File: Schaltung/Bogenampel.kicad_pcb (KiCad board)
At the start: 2 copper layers, 95 x 62 mm, 32 parts, among them J1 Input 1, J10 Display, J2 Input 2, J3 Input 3, J4 Input 4, J5 Input 5, J6 Power Bank, J7 Battery, J8 KY-006, J9 WS2812B Stripe Timer, U1 NRF24L01_Breakout, U2 TXS0108EPW

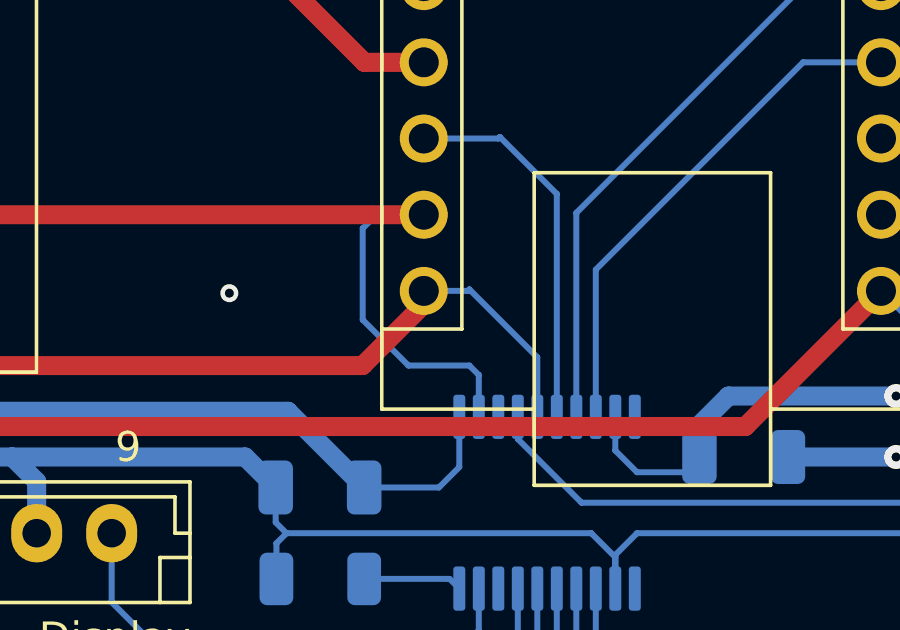
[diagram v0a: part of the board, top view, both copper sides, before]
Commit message: Fix: NRF24L01 Funkverbindung - Konfiguration korrigiert
Mehrere kritische Probleme behoben:

1. Payload-Größe synchronisiert
   - Sender: 4 Bytes → 2 Bytes (passend zu RadioPacket)
   - Empfänger: bereits korrekt 2 Bytes

2. Pin-Initialisierung korrigiert
   - Entfernt manuelle CE/CSN Pin-Init (RF24.begin() macht das)
   - Verhindert Konflikte mit RF24-Bibliothek

3. SPI-Bus-Initialisierung optimiert (Sender)
   - SPI.begin() einmal am Anfang von setup()
   - Radio VOR Display initialisieren (verhindert SPI-Konflikte)
   - Doppelte SPI.begin() Aufrufe entfernt

4. RF24-Enums direkt verwendet
   - Entfernt custom DataRate/PowerLevel Enums
   - Verwendet rf24_datarate_e und rf24_pa_dbm_e direkt
   - Behebt Type-Cast Probleme

5. Namenskonflikte behoben
   - Groups::Type::CD → Groups::Type::GROUP_CD
   - Konflikt mit RF24 Makro #define CD 0x09

6. Debug-Ausgaben erweitert
   - Manuelle Radio-Diagnose hinzugefügt
   - isChipConnected(), getChannel(), etc.

Hardware-Problem identifiziert:
- NRF24L01 benötigt 3.3V (nicht 5V!)
- Kondensator 10-100µF empfohlen
- Evtl. Level-Shifter für 5V↔3.3V Logik nötig

🤖 Generated with [Claude Code](https://claude.com/claude-code)

Co-Authored-By: Claude Sonnet 4.5 <noreply@anthropic.com>
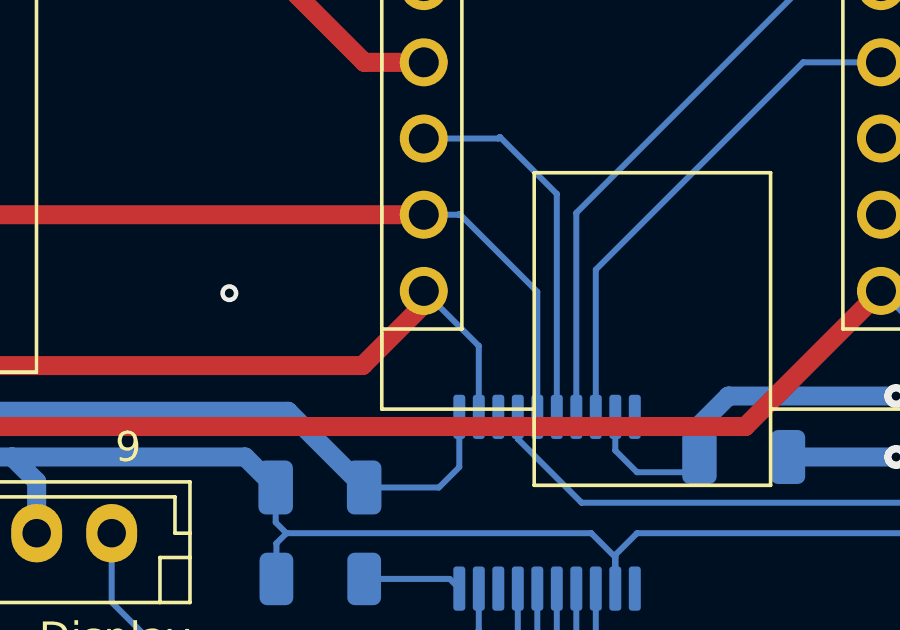
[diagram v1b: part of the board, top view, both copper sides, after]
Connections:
- A2 pad 14: /SPI.MISO -> /SPI.MOSI
- A2 pad 15: /SPI.MOSI -> /SPI.MISO
- U1 pad 6: /SPI.MISO -> /SPI.MOSI
- U1 pad 7: /SPI.MOSI -> /SPI.MISO
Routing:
- net /SPI.MOSI: track 52.9 -> 48.3 mm
- net /SPI.MISO: track 50.6 -> 51.1 mm
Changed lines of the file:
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@@
 			(layers "*.Cu" "*.Mask")
 			(remove_unused_layers no)
-			(net 5 "/SPI.MISO")
+			(net 21 "/SPI.MOSI")
 			(pinfunction "MOSI")
 			(pintype "input")
@@
 			(layers "*.Cu" "*.Mask")
 			(remove_unused_layers no)
-			(net 21 "/SPI.MOSI")
+			(net 5 "/SPI.MISO")
 			(pinfunction "MISO")
 			(pintype "output")
@@
 			(layers "*.Cu" "*.Mask")
 			(remove_unused_layers no)
-			(net 5 "/SPI.MISO")
+			(net 21 "/SPI.MOSI")
 			(pinfunction "D11")
 			(pintype "bidirectional")
@@
 			(layers "*.Cu" "*.Mask")
 			(remove_unused_layers no)
-			(net 21 "/SPI.MOSI")
+			(net 5 "/SPI.MISO")
 			(pinfunction "D12")
 			(pintype "bidirectional")
@@
 	)
 	(segment
-		(start 100.263 86.439)
-		(end 98.6865 86.439)
+		(start 136.656 92)
+		(end 136.656 92.452)
 		(width 0.635)
 		(layer "F.Cu")
@@
 	)
 	(segment
-		(start 103.284 89.46)
-		(end 100.263 86.439)
+		(start 98.152 94.488)
+		(end 96.1465 92.4825)
 		(width 0.635)
 		(layer "F.Cu")
@@
 	)
 	(segment
-		(start 136.656 89.46)
-		(end 103.284 89.46)
+		(start 134.62 94.488)
+		(end 98.152 94.488)
 		(width 0.635)
 		(layer "F.Cu")
@@
 	)
 	(segment
-		(start 135.18 89.46)
-		(end 136.656 89.46)
-		(width 0.2)
-		(layer "B.Cu")
-		(net 5)
-	)
-	(segment
-		(start 138.49 94.802)
-		(end 138.176 94.488)
-		(width 0.2)
-		(layer "B.Cu")
-		(net 5)
-	)
-	(segment
-		(start 134.62 92.964)
-		(end 134.62 89.916)
-		(width 0.2)
-		(layer "B.Cu")
-		(net 5)
-	)
-	(segment
-		(start 134.62 89.916)
-		(end 135.128 89.408)
-		(width 0.2)
-		(layer "B.Cu")
+		(start 136.656 92.452)
+		(end 134.62 94.488)
+		(width 0.635)
+		(layer "F.Cu")
 		(net 5)
 	)
 	(segment
-		(start 135.128 89.408)
-		(end 135.18 89.46)
-		(width 0.2)
-		(layer "B.Cu")
+		(start 96.1465 92.4825)
+		(end 96.1465 88.979)
+		(width 0.635)
+		(layer "F.Cu")
 		(net 5)
 	)
 	(segment
 		(start 138.49 96.1975)
-		(end 138.49 94.802)
-		(width 0.2)
-		(layer "B.Cu")
-		(net 5)
-	)
-	(segment
-		(start 138.176 94.488)
-		(end 136.144 94.488)
+		(end 138.49 93.834)
 		(width 0.2)
 		(layer "B.Cu")
@@
 	)
 	(segment
-		(start 136.144 94.488)
-		(end 134.62 92.964)
+		(start 138.49 93.834)
+		(end 136.656 92)
 		(width 0.2)
 		(layer "B.Cu")
@@
 	)
 	(segment
-		(start 136.656 92)
-		(end 136.656 92.452)
-		(width 0.635)
-		(layer "F.Cu")
-		(net 21)
-	)
-	(segment
-		(start 98.152 94.488)
-		(end 96.1465 92.4825)
-		(width 0.635)
-		(layer "F.Cu")
-		(net 21)
-	)
-	(segment
-		(start 134.62 94.488)
-		(end 98.152 94.488)
+		(start 100.263 86.439)
+		(end 98.6865 86.439)
 		(width 0.635)
 		(layer "F.Cu")
@@
 	)
 	(segment
-		(start 136.656 92.452)
-		(end 134.62 94.488)
+		(start 103.284 89.46)
+		(end 100.263 86.439)
 		(width 0.635)
 		(layer "F.Cu")
@@
 	)
 	(segment
-		(start 96.1465 92.4825)
-		(end 96.1465 88.979)
+		(start 136.656 89.46)
+		(end 103.284 89.46)
 		(width 0.635)
 		(layer "F.Cu")
@@
 	)
 	(segment
-		(start 138.176 91.948)
-		(end 138.124 92)
+		(start 137.8458 89.4334)
+		(end 137.8192 89.46)
 		(width 0.2)
 		(layer "B.Cu")
@@
 	)
 	(segment
-		(start 138.124 92)
-		(end 136.656 92)
+		(start 137.8192 89.46)
+		(end 136.656 89.46)
 		(width 0.2)
 		(layer "B.Cu")
@@
 	)
 	(segment
-		(start 140.44 96.1975)
-		(end 140.44 94.212)
+		(start 140.44 92.0276)
+		(end 137.8458 89.4334)
 		(width 0.2)
 		(layer "B.Cu")
@@
 	)
 	(segment
-		(start 140.44 94.212)
-		(end 138.176 91.948)
+		(start 140.44 96.1975)
+		(end 140.44 92.0276)
 		(width 0.2)
 		(layer "B.Cu")

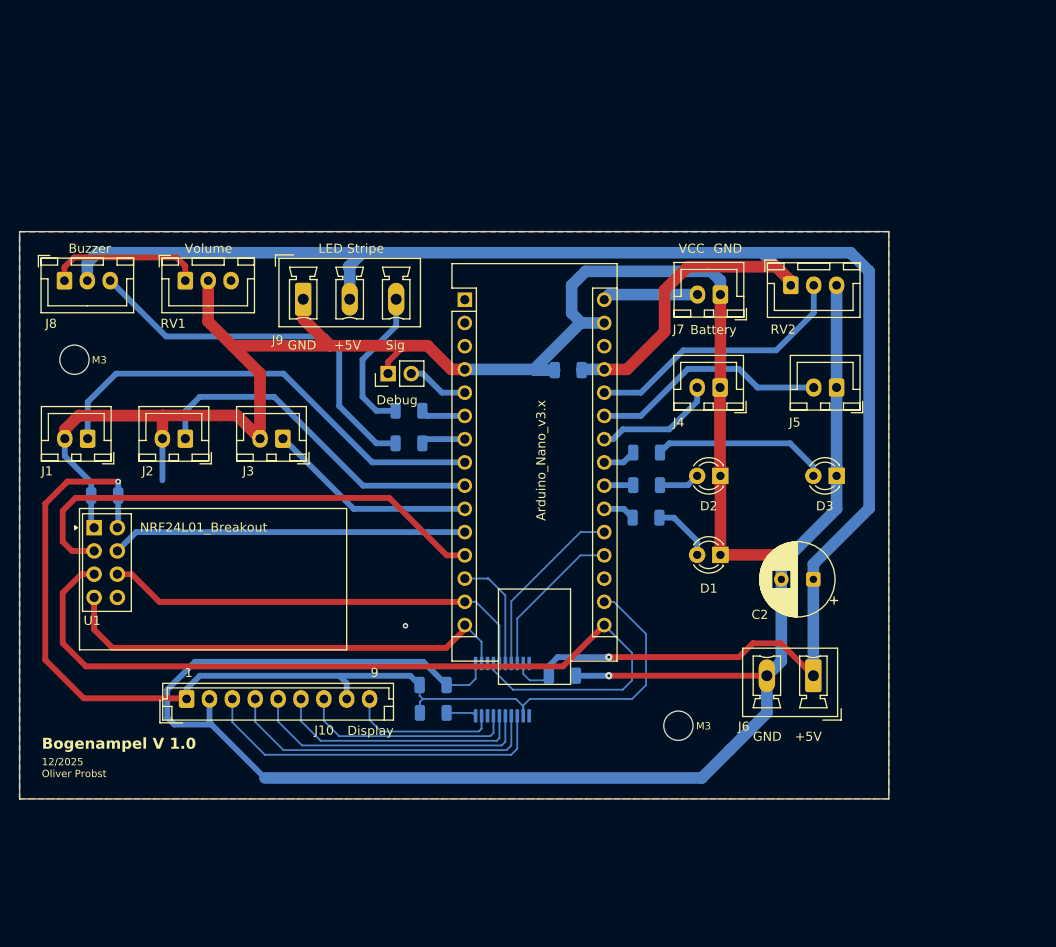
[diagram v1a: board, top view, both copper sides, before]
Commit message: UI-Verbesserungen und Funk-Debugging
Schießbetrieb UI:
- Überschrift in Orange mit Trennlinie
- Timer horizontal zentriert und nur 1x pro Sekunde aktualisiert
- Layout-Abstände optimiert (weniger gestaucht)
- Button "Passe beenden" mit grauem Hintergrund
- Bei 3-4 Schützen: Timer tiefer positioniert

Gruppenanzeige:
- Vereinheitlichtes Format für PfeileHolenMenu und Schießbetrieb
- Statischer String "{A/B -> C/D} {C/D -> A/B}"
- Aktuelle Gruppe gelb hervorgehoben, Rest grau
- "Nächste:" in PfeileHolenMenu, "Aktuell:" in Schießbetrieb

Funk-Debugging:
- Kontinuierliche PING-Tests im Splash Screen (alle 2 Sek)
- Pipe-Adresse wird beim Start ausgegeben
- Versucht printDetails() mit Serial.flush()
- Empfänger auf Pipe 1 umgestellt (statt Pipe 0)

🤖 Generated with [Claude Code](https://claude.com/claude-code)

Co-Authored-By: Claude Sonnet 4.5 <noreply@anthropic.com>
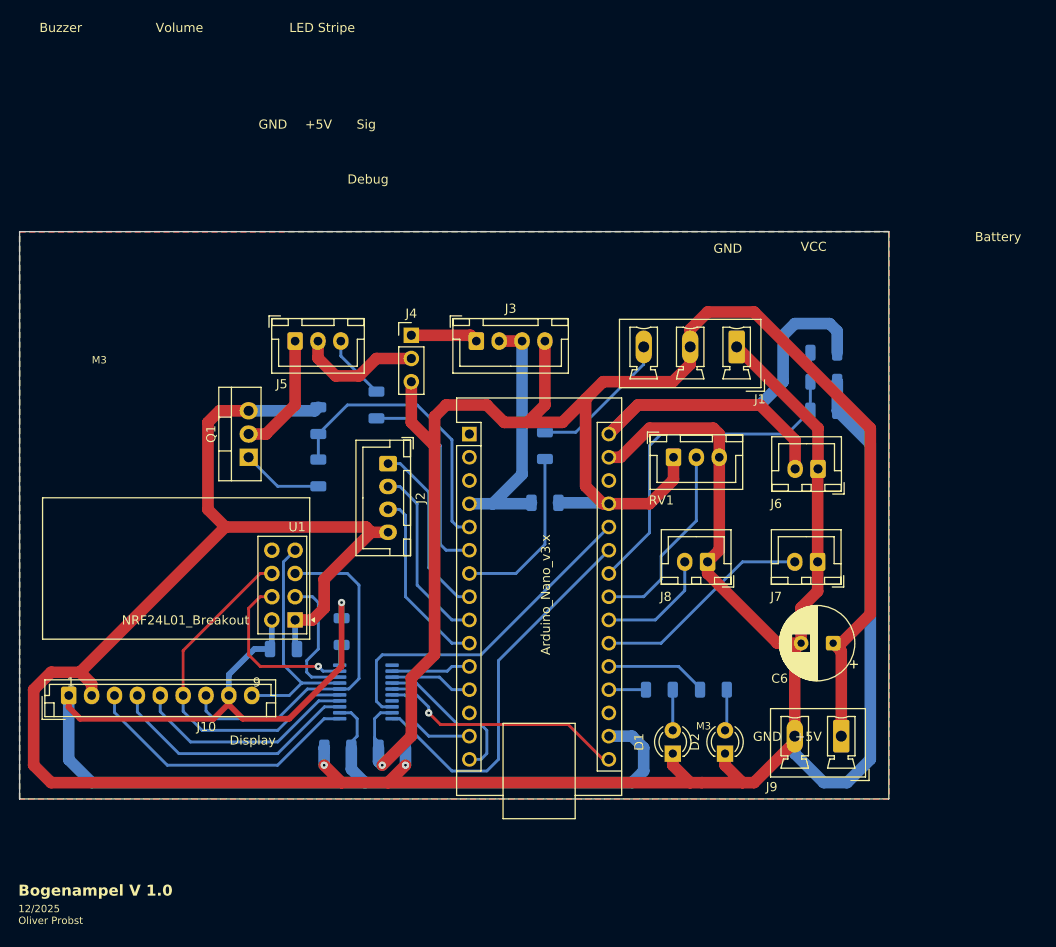
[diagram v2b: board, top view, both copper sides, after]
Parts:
- removed D3: LED, LED_THT:LED_D3.0mm
- removed the J9 at (119.0, 56.4)
- removed JD1: Debug, Connector_PinHeader_2.54mm:PinHeader_1x02_P2.54mm_Vertical
- removed REF** (x2): MountingHole_3.2mm_M3_ISO14580, MountingHole:MountingHole_3.2mm_M3_ISO14580
- removed RV2: Input 6, Connector_JST:JST_XH_B3B-XH-A_1x03_P2.50mm_Vertical
- added C3: 100nF, Capacitor_SMD:C_1206_3216Metric, B.Cu at (175.9, 68.6)
- added J4: Jumper: 5V/Ext Voltage, Connector_PinHeader_2.54mm:PinHeader_1x03_P2.54mm_Vertical, F.Cu at (130.8, 60.3)
- added Q1: IRLZ44N, Package_TO_SOT_THT:TO-220-3_Vertical, F.Cu at (113.0, 73.7)
- added R2: 100Ω, Resistor_SMD:R_1206_3216Metric, B.Cu at (127.0, 67.9)
- added R7: 10kΩ, Resistor_SMD:R_1206_3216Metric, B.Cu at (175.9, 62.2)
- added R8: 10kΩ, Resistor_SMD:R_1206_3216Metric, B.Cu at (175.9, 65.4)
- C6: renamed from C2; value 1000µF -> 470µF
- J1: value Input 1 -> WS2812B Stripe Timer; footprint Connector_JST:JST_XH_B2B-XH-A_1x02_P2.50mm_Vertical -> Connector_Phoenix_MC_HighVoltage:PhoenixContact_MCV_1,5_3-G-5.08_1x03_P5.08mm_Vertical
- J2: value Input 2 -> Conn_01x04_Pin; footprint Connector_JST:JST_XH_B2B-XH-A_1x02_P2.50mm_Vertical -> Connector_JST:JST_XH_B4B-XH-A_1x04_P2.50mm_Vertical
- J3: value Input 3 -> DC/DC Boost; footprint Connector_JST:JST_XH_B2B-XH-A_1x02_P2.50mm_Vertical -> Connector_JST:JST_XH_B4B-XH-A_1x04_P2.50mm_Vertical
- J5: renamed from J8; value KY-006 -> Buzzer
- R3: renamed from R5; value 100Ω -> 220Ω
- R4: renamed from R3; value 330Ω -> 100kΩ
- RV1: value R_Potentiometer -> Input 6
- moved J1 71.6 mm to (166.4, 61.6)
- moved RV1 56.7 mm to (159.5, 73.7)
- moved R4 36.0 mm to (120.7, 69.7), turned to -90 degrees
- moved D2 30.4 mm to (165.1, 106.0), turned to 90 degrees
- moved J5 26.1 mm to (118.1, 61.0)
- moved C1 25.8 mm to (116.8, 94.6), turned to 0 degrees
- moved U1 24.2 mm to (118.1, 91.4), turned to 180 degrees
- moved J8 23.7 mm to (163.2, 85.1)
- moved J3 23.7 mm to (137.9, 61.0), turned to 0 degrees
- moved R6 23.5 mm to (163.8, 99.1)
- moved D1 22.3 mm to (159.4, 106.0), turned to 90 degrees
- moved J2 22.3 mm to (128.3, 74.4), turned to -90 degrees
- moved J7 21.8 mm to (175.2, 85.1)
- moved J6 21.8 mm to (175.3, 74.9)
- moved C4 20.2 mm to (128.7, 105.4)
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- renumbered A2 to A1, C5 to C2, C3 to C4, C4 to C5, J7 to J6, J4 to J7, J5 to J8, J6 to J9, R4 to R1, R1 to R5, R2 to R6, R6 to R9
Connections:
- A1 pad 10: Net-(A2-D7) -> /DI3
- A1 pad 11: /CS_NRF -> /NRF_CSN_5V
- A1 pad 12: /CE_NRF -> /NRF_CS_5V
- A1 pad 13: /UI_DC/RS -> /DSPL_DC_5V
- A1 pad 14: /SPI.MOSI -> /SPI_5V.MOSI
- A1 pad 15: /SPI.MISO -> /SPI_5V.MISO
- A1 pad 16: /SPI.SCK -> /SPI_5V.SCK
- A1 pad 19: /<NO NET> -> /SIG_LED1
- A1 pad 20: /UI_RES -> /SIG_LED2
- A1 pad 21: Net-(A2-A2) -> /DI4
- A1 pad 22: Net-(A2-A3) -> /DI5
- A1 pad 23: Net-(A2-A4) -> /AI1
- A1 pad 24: Net-(A2-A5) -> /BAT_MON
- A1 pad 25: Net-(A2-A6) -> /DSPL_CS_5V
- A1 pad 26: Net-(A2-A7) -> /DSPL_RES_5V
- A1 pad 29: -BATT -> GND
- A1 pad 4: -BATT -> GND
- A1 pad 5: Net-(A2-D2) -> Net-(A1-D2)
- A1 pad 6: Net-(A2-D3) -> Net-(A1-D3)
- A1 pad 7: Net-(A2-D4) -> Net-(A1-D4)
- A1 pad 8: Net-(A2-D5) -> /DI1
- A1 pad 9: Net-(A2-D6) -> /DI2
- C1 pad 2: -BATT -> GND
- C2 pad 2: -BATT -> GND
- C4 pad 1: -BATT -> GND
- C5 pad 2: -BATT -> GND
- C6 pad 2: -BATT -> GND
- D1 pad 1: -BATT -> GND
- D2 pad 1: -BATT -> GND
- J1 pad 1: Net-(A2-D5) -> GND
- J1 pad 2: -BATT -> +5V
- J10 pad 2: -BATT -> GND
- J10 pad 3: /DSPL_CS -> /DSPL_CS_3V3
- J10 pad 4: /DSPL_RES -> /DSPL_RS_3V3
- J10 pad 5: /DSPL_DC/RS -> /DSPL_DC_3V3
- J10 pad 6: /DSPL_MOSI -> /SPI_3V3.MOSI
- J10 pad 7: /DSPL_SCK -> /SPI_3V3.SCK
- J10 pad 9: /DSPL_MISO -> /SPI_3V3.MISO
- J2 pad 1: Net-(A2-D6) -> /DI1
- J2 pad 2: -BATT -> /DI2
- J3 pad 1: Net-(A2-D7) -> Net-(J3-Pin_1)
- J3 pad 2: -BATT -> GND
- J5 pad 1: Net-(J8-Pin_1) -> Net-(J5-Pin_1)
- J5 pad 2: +5V -> Net-(J4-Pin_2)
- J5 pad 3: Net-(J8-Pin_3) -> Net-(J5-Pin_3)
- J6 pad 1: -BATT -> GND
- J7 pad 1: -BATT -> GND
- J7 pad 2: Net-(A2-A5) -> /DI4
- J8 pad 1: -BATT -> GND
- J8 pad 2: Net-(A2-A6) -> /DI5
- J9 pad 2: -BATT -> GND
- R1 pad 1: Net-(A2-D3) -> Net-(A1-D4)
- R1 pad 2: Net-(J9-Pin_3) -> Net-(J1-Pin_3)
- R3 pad 1: Net-(A2-D4) -> Net-(A1-D2)
- R3 pad 2: Net-(J8-Pin_3) -> Net-(Q1-G)
- R4 pad 1: Net-(A2-A4) -> GND
- R4 pad 2: Net-(D3-A) -> Net-(A1-D2)
- R5 pad 1: Net-(A2-A2) -> /SIG_LED1
- R6 pad 1: Net-(A2-A3) -> /SIG_LED2
- RV1 pad 1: Net-(J8-Pin_1) -> +5V
- RV1 pad 2: -BATT -> /AI1
- RV1 pad 3: unconnected-(RV1-Pad3) -> GND
- U1 pad 1: -BATT -> GND
- U1 pad 3: /CE_NRF -> /NRF_CS_3V3
- U1 pad 4: /CS_NRF -> /NRF_CSN_3V3
- U1 pad 5: /SPI.SCK -> /SPI_3V3.SCK
- U1 pad 6: /SPI.MOSI -> /SPI_3V3.MOSI
- U1 pad 7: /SPI.MISO -> /SPI_3V3.MISO
- U2 pad 1: unconnected-(U2-A1-Pad1) -> /DSPL_CS_3V3
- U2 pad 11: -BATT -> GND
- U2 pad 12: /SPI.MISO -> /NRF_CSN_5V
- U2 pad 13: unconnected-(U2-B7-Pad13) -> /NRF_CS_5V
- U2 pad 14: /SPI.SCK -> /SPI_5V.MISO
- U2 pad 15: /SPI.MOSI -> /SPI_5V.SCK
- U2 pad 16: /UI_DC/RS -> /SPI_5V.MOSI
- U2 pad 17: /UI_RES -> /DSPL_DC_5V
- U2 pad 18: /<NO NET> -> /DSPL_RES_5V
- U2 pad 20: unconnected-(U2-B1-Pad20) -> /DSPL_CS_5V
- U2 pad 3: /DSPL_CS -> /DSPL_RS_3V3
- U2 pad 4: /DSPL_RES -> /DSPL_DC_3V3
- U2 pad 5: /DSPL_DC/RS -> /SPI_3V3.MOSI
- U2 pad 6: /DSPL_MOSI -> /SPI_3V3.SCK
- U2 pad 7: /DSPL_SCK -> /SPI_3V3.MISO
- U2 pad 8: unconnected-(U2-A7-Pad8) -> /NRF_CS_3V3
- U2 pad 9: /DSPL_MISO -> /NRF_CSN_3V3
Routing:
- net GND: track 0.00 -> 377.4 mm, vias 0 -> 2
- net -BATT: track 362.3 -> 0.00 mm, vias 2 -> 0
- net /SPI.SCK: track 96.4 -> 0.00 mm
- net /CE_NRF: track 54.4 -> 0.00 mm
- net +BATT: track 10.4 -> 62.0 mm
- net /SPI.MISO: track 51.1 -> 0.00 mm
- net Net-(A2-D5): track 50.5 -> 0.00 mm
- net /SPI.MOSI: track 48.3 -> 0.00 mm
- net /DSPL_CS_5V: track 0.00 -> 42.4 mm
- net Net-(J8-Pin_3): track 42.1 -> 0.00 mm
- net /BAT_MON: track 0.00 -> 41.3 mm
- net /SPI_3V3.MOSI: track 0.00 -> 39.4 mm
- net /DSPL_CS: track 39.0 -> 0.00 mm
- net /CS_NRF: track 38.8 -> 0.00 mm
- net /SPI_3V3.SCK: track 0.00 -> 38.3 mm
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- added copper zone on B.Cu, net GND
- added copper zone on F.Cu, net GND
- removed copper zone on B.Cu, net -BATT
- removed copper zone on F.Cu, net -BATT
